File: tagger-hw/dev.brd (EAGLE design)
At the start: 65.7 x 62.2 mm, 50 parts, among them J2 22-23-2021, J3 22-23-2021, X1 EXC-31B

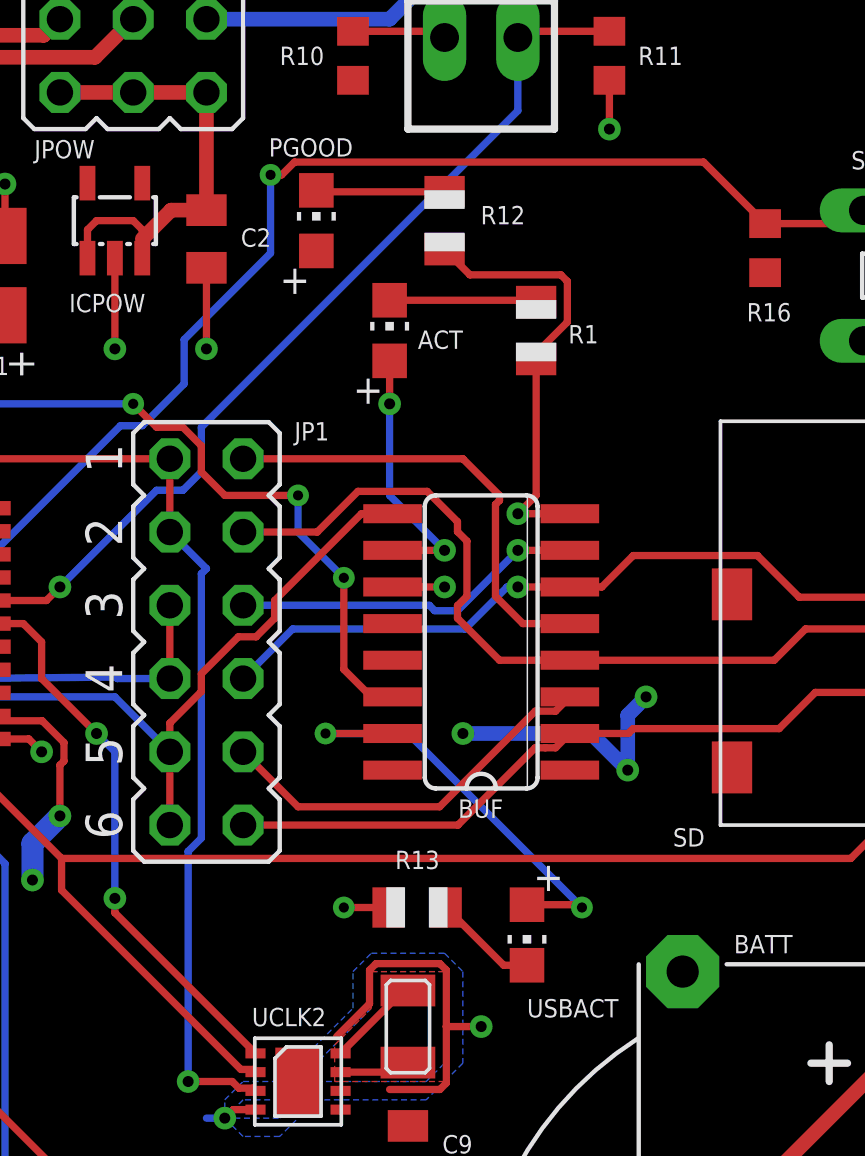
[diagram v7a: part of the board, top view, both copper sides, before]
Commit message: Fix some package sizes (0805 -> 0603)
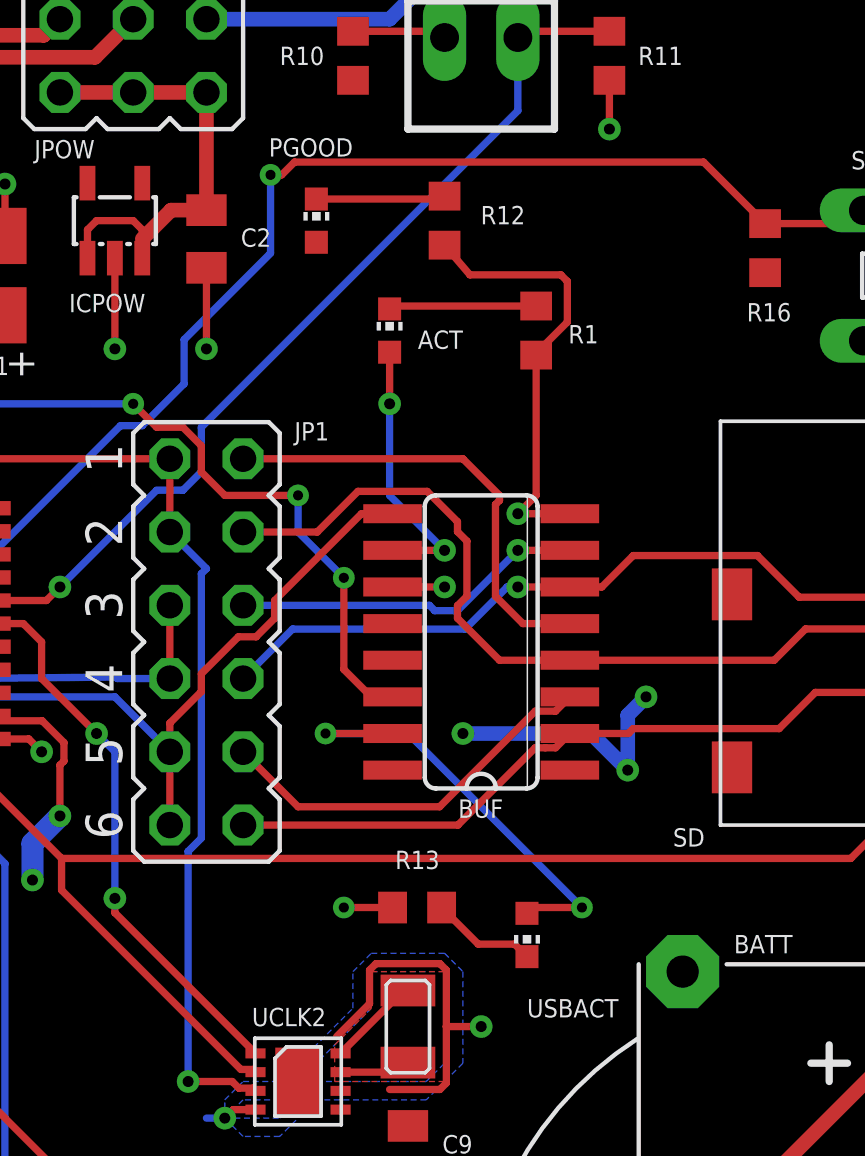
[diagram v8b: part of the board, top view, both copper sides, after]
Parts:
- ACT, PGOOD, USBACT: device adafruit:CHIP-LED0805 -> adafruit:CHIP-LED0603
- R1, R12, R13: device adafruit:R0805 -> adafruit:R0603
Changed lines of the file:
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@@
 </autorouter>
 <elements>
-<element name="ACT" library="adafruit" package="CHIP-LED0805" value="RED" x="37.465" y="48.26" smashed="yes">
+<element name="ACT" library="adafruit" package="CHIP-LED0603" value="RED" x="37.465" y="48.26" smashed="yes">
 <attribute name="NAME" x="40.005" y="48.26" size="0.635" layer="25" font="vector" rot="R180"/>
 <attribute name="VALUE" x="40.005" y="46.99" size="0.635" layer="27" font="vector" rot="R90"/>
@@
 <attribute name="VALUE" x="26.035" y="48.641" size="0.635" layer="27" font="vector"/>
 </element>
-<element name="R1" library="adafruit" package="R0805" value="1K" x="42.545" y="48.26" smashed="yes" rot="R90">
+<element name="R1" library="adafruit" package="R0603" value="1K" x="42.545" y="48.26" smashed="yes" rot="R90">
 <attribute name="NAME" x="44.704" y="48.4505" size="0.635" layer="25" font="vector" rot="R180"/>
 <attribute name="VALUE" x="44.831" y="47.498" size="0.635" layer="27" font="vector" rot="R90"/>
@@
 <attribute name="VALUE" x="20.32" y="7.747" size="1.27" layer="27" ratio="10" rot="R90"/>
 </element>
-<element name="PGOOD" library="adafruit" package="CHIP-LED0805" value="GREEN" x="34.925" y="52.07" smashed="yes">
+<element name="PGOOD" library="adafruit" package="CHIP-LED0603" value="GREEN" x="34.925" y="52.07" smashed="yes">
 <attribute name="NAME" x="36.195" y="54.9275" size="0.635" layer="25" font="vector" rot="R180"/>
 <attribute name="VALUE" x="37.465" y="50.8" size="1.27" layer="27" rot="R90"/>
 </element>
-<element name="R12" library="adafruit" package="R0805" value="1K" x="39.37" y="52.07" smashed="yes" rot="R90">
+<element name="R12" library="adafruit" package="R0603" value="1K" x="39.37" y="52.07" smashed="yes" rot="R90">
 <attribute name="NAME" x="42.164" y="52.578" size="0.635" layer="25" font="vector" rot="R180"/>
 <attribute name="VALUE" x="41.656" y="51.308" size="1.27" layer="27" rot="R90"/>
 </element>
-<element name="USBACT" library="adafruit" package="CHIP-LED0805" value="GREEN" x="42.2275" y="27.305" smashed="yes" rot="R180">
+<element name="USBACT" library="adafruit" package="CHIP-LED0603" value="GREEN" x="42.2275" y="27.305" smashed="yes" rot="R180">
 <attribute name="NAME" x="42.2275" y="24.4475" size="0.635" layer="25" font="vector"/>
 <attribute name="VALUE" x="39.6875" y="28.575" size="1.27" layer="27" rot="R270"/>
 </element>
-<element name="R13" library="adafruit" package="R0805" value="1K" x="38.4175" y="28.2575" smashed="yes">
+<element name="R13" library="adafruit" package="R0603" value="1K" x="38.4175" y="28.2575" smashed="yes">
 <attribute name="NAME" x="37.6555" y="29.591" size="0.635" layer="25" font="vector"/>
 <attribute name="VALUE" x="37.6555" y="25.9715" size="1.27" layer="27"/>
@@
 <wire x1="43.7134" y1="41.91" x2="41.91" y2="41.91" width="0.254" layer="1"/>
 <via x="41.91" y="41.91" extent="1-16" drill="0.381"/>
-<wire x1="42.545" y1="47.26" x2="42.545" y2="42.545" width="0.254" layer="1"/>
+<wire x1="42.545" y1="47.41" x2="42.545" y2="42.545" width="0.254" layer="1"/>
 <wire x1="42.545" y1="42.545" x2="41.91" y2="41.91" width="0.254" layer="1"/>
 <via x="8.89" y="14.2875" extent="1-16" drill="0.381"/>
@@
 <wire x1="43.4028125" y1="50.191" x2="43.626" y2="49.9678125" width="0.254" layer="1"/>
 <wire x1="43.626" y1="49.9678125" x2="43.626" y2="48.5521875" width="0.254" layer="1"/>
-<wire x1="42.545" y1="47.4711875" x2="42.545" y2="47.26" width="0.254" layer="1"/>
+<wire x1="42.545" y1="47.4711875" x2="42.545" y2="47.41" width="0.254" layer="1"/>
 <wire x1="43.626" y1="48.5521875" x2="42.545" y2="47.4711875" width="0.254" layer="1"/>
-<wire x1="39.37" y1="51.07" x2="40.249" y2="50.191" width="0.254" layer="1"/>
+<wire x1="39.37" y1="51.22" x2="40.249" y2="50.191" width="0.254" layer="1"/>
 <wire x1="40.249" y1="50.191" x2="43.4028125" y2="50.191" width="0.254" layer="1"/>
-<wire x1="37.4175" y1="28.2575" x2="35.8775" y2="28.2575" width="0.254" layer="1"/>
+<wire x1="37.5675" y1="28.2575" x2="35.8775" y2="28.2575" width="0.254" layer="1"/>
 <via x="35.8775" y="28.2575" extent="1-16" drill="0.35" diameter="0.381"/>
 <contactref element="S2" pad="4"/>
@@
 <contactref element="ACT" pad="C"/>
 <contactref element="R1" pad="2"/>
-<wire x1="37.465" y1="49.31" x2="42.495" y2="49.31" width="0.254" layer="1"/>
-<wire x1="42.495" y1="49.31" x2="42.545" y2="49.26" width="0.254" layer="1"/>
+<wire x1="42.495" y1="49.31" x2="42.545" y2="49.11" width="0.254" layer="1"/>
+<wire x1="37.465" y1="49.01" x2="37.565" y2="49.11" width="0.254" layer="1"/>
+<wire x1="37.565" y1="49.11" x2="42.545" y2="49.11" width="0.254" layer="1"/>
 </signal>
 <signal name="MOSI">
@@
 <wire x1="37.465" y1="42.545" x2="37.465" y2="45.72" width="0.254" layer="16"/>
 <via x="37.465" y="45.72" extent="1-16" drill="0.381"/>
-<wire x1="37.465" y1="45.72" x2="37.465" y2="47.21" width="0.254" layer="1"/>
+<wire x1="37.465" y1="45.72" x2="37.465" y2="47.51" width="0.254" layer="1"/>
 </signal>
 <signal name="MOSI_BUF">
@@
 <contactref element="R12" pad="2"/>
 <contactref element="PGOOD" pad="C"/>
-<wire x1="34.925" y1="53.12" x2="34.975" y2="53.07" width="0.254" layer="1"/>
-<wire x1="34.975" y1="53.07" x2="39.37" y2="53.07" width="0.254" layer="1"/>
+<wire x1="34.925" y1="52.82" x2="39.27" y2="52.82" width="0.254" layer="1"/>
+<wire x1="39.27" y1="52.82" x2="39.37" y2="52.92" width="0.254" layer="1"/>
 </signal>
 <signal name="D+_BUF">
@@
 <via x="44.1325" y="28.2575" extent="1-16" drill="0.35" diameter="0.381"/>
 <wire x1="44.1325" y1="28.2575" x2="44.035" y2="28.355" width="0.254" layer="1"/>
-<wire x1="44.035" y1="28.355" x2="42.2275" y2="28.355" width="0.254" layer="1"/>
+<wire x1="44.1325" y1="28.2575" x2="42.43" y2="28.2575" width="0.254" layer="1"/>
+<wire x1="42.43" y1="28.2575" x2="42.2275" y2="28.055" width="0.254" layer="1"/>
 </signal>
 <signal name="D+_BUF_D">
 <contactref element="R13" pad="2"/>
 <contactref element="USBACT" pad="C"/>
-<wire x1="39.4175" y1="28.2575" x2="41.42" y2="26.255" width="0.254" layer="1"/>
-<wire x1="41.42" y1="26.255" x2="42.2275" y2="26.255" width="0.254" layer="1"/>
+<wire x1="42.2275" y1="26.555" x2="41.795" y2="26.9875" width="0.254" layer="1"/>
+<wire x1="40.5375" y1="26.9875" x2="39.2675" y2="28.2575" width="0.254" layer="1"/>
+<wire x1="41.795" y1="26.9875" x2="40.5375" y2="26.9875" width="0.254" layer="1"/>
 </signal>
 <signal name="BTN1">
